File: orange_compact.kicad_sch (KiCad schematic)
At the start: 303 parts, among them IC1 MCP25625-E_ML, IC2 MIC5317-1.8YD5-TR, IC3 CD4060BPWR, IC4 MAX13487EESA+T, IC5 MCP73833T-FCI/MF, J1 Battery, J4 Conn_Coaxial, J4 USB_B_Micro, J5 Conn_01x08_Pin, J6 USB_B_Micro, Q1 MMBT3904, Q12 Q_NPN_BEC_BRT, Q2 MMBT3904, Q2 Q_NPN_BEC_BRT, Q3 MMBT3904, Q5 Q_NPN_BEC_BRT, Q6 Q_NPN_BEC_BRT, Q8 Q_NPN_BEC_BRT, SW1 SW_Push, SW2 SW_Push, U1 EG916QGLLG-N03-SGNSA, U10 LP5907MFX-3.3, U11 LM3671MF-3.3/NOPB, U12 AMS1117-1.8, U13 LIS2DH12TR, U14 LP5907MFX-1.8, U15 LM66100DCKR, U16 LM66100DCKR, U17 TPS3828-33DBVRG4, U18 TPS61022, U2 MDBT50Q-1M, U20 TPS566242DRLR, U21 SN74LVC1G14DBV, U22 TP4056, U23 MCP2515-xST, U24 MCP2562-E-MF, U25 ESP32-S3-MINI-1, U26 MCP2562-E/MF, U29 TXB0108RGY, U3 FDMC86139P, U30 TXB0104RUT, U4 LM5012DDAR, U6 LMR14030SDDAR, U7 LP5907MFX-3.3, U8 1NCE IoT SIMs Chip, U9 USBLC6-2SC6, Y1 16MHz

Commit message: done before gnd optimization
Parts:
- removed J5: Conn_01x08_Pin, Connector_JST:JST_XH_S8B-XH-A_1x08_P2.50mm_Horizontal, symbol Connector:Conn_01x08_Pin
- removed L12: 1uH, Inductor_SMD:L_Coilcraft_XAL4020-XXX, symbol Device:L
- removed L14: L_Ferrite_Coupled_1243, Inductor_SMD:L_CommonModeChoke_Laird_CMA0805, symbol Device:L_Ferrite_Coupled_1243
- removed R51: 22k, Resistor_SMD:R_0805_2012Metric, symbol Device:R_Small
- removed R55, R56: 0, Resistor_SMD:R_0402_1005Metric, symbol Device:R
- removed TH1: DNP, Resistor_SMD:R_0603_1608Metric, symbol Device:Thermistor_NTC
- added C119, C120: 1uF, Capacitor_SMD:C_0402_1005Metric, symbol Device:C
- added C72, C73: 100nF, Capacitor_SMD:C_0402_1005Metric, symbol Device:C
- added D17: BAT54AW, Package_TO_SOT_SMD:SOT-323_SC-70, symbol Diode:BAT54AW
- added D18: SM712_SOT23, Package_TO_SOT_SMD:SOT-323_SC-70, symbol Diode:SM712_SOT23
- added D20, D21, D22, D24: D4V5H1BS2LP-7B, Diode_SMD:D_0402_1005Metric, symbol Device:D_Zener
- added J7: Conn_01x11_Pin, Connector_PinHeader_2.00mm:PinHeader_1x11_P2.00mm_Vertical, symbol Connector:Conn_01x11_Pin
- added L15: 2.2uH, Inductor_SMD:L_0603_1608Metric, symbol Device:L
- added R57: 680, Resistor_SMD:R_0805_2012Metric, symbol Device:R_Small
- added R60: 1k, Resistor_SMD:R_0402_1005Metric, symbol Device:R_Small
- added R61: 130, Resistor_SMD:R_0603_1608Metric, symbol Device:R_Small
- added TP18: TestPoint, TestPoint:TestPoint_Pad_D1.0mm, symbol Connector:TestPoint
- added U19, U5: LTV-217, Package_SO:SOIC-4_4.55x2.6mm_P1.27mm, symbol TC-ICs:LTV-217
- added U27: LP5907MFX-3.3, Package_TO_SOT_SMD:SOT-23-5, symbol Regulator_Linear:LP5907MFX-3.3
- added U28: USBLC6-2SC6, Package_TO_SOT_SMD:SOT-23-6, symbol Power_Protection:USBLC6-2SC6
- D10: footprint Package_TO_SOT_SMD:TO-277A_alt -> Diode_SMD:D_SMA; MPN V8P12-M3/86A -> RB058L150; desc DIODE SCHOTTKY 120V 8A TO277A -> DIODE SCHOTTKY 150V 3A PMDS
- R31: footprint Resistor_SMD:R_0805_2012Metric -> Resistor_SMD:R_0603_1608Metric; MPN RMCF0805FT330K -> 0603WAF3303T5E
- R32: value 22k -> 11k; footprint Resistor_SMD:R_0805_2012Metric -> Resistor_SMD:R_0603_1608Metric; MPN RMCF0805FT22K0 -> RTT031102FTP
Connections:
- net 3V3_ALWAYS_ON: no longer C112.2, C44.1, C45.1, JP3.1 (A), R37.1, R38.1, R58.2, R59.2, R60.2, U13.10 (VDD_IO), U13.2 (CS), U13.9 (VDD), U26.5 (Vio)
- net 4V7_BOOST: now also TP16.1
- net 5V0: now also C119.1, U27.1 (IN)
- net CAN_500_H: now also D12.1 (A1), U26.7 (CANH), J7.7 (Pin_7); no longer D12.2 (A2)
- net CAN_500_L: now also D12.2 (A2), U26.6 (CANL), J7.6 (Pin_6); no longer D12.1 (A1)
- net D+/A: now also J7.8 (Pin_8)
- net D-/B: now also J7.9 (Pin_9)
- net GND: now also TP17.1, C119.2, C120.2, C72.2, C73.2, D17.3, D18.3 (common), D20.2 (A), D21.2 (A), D22.2 (A), D24.2 (A), J7.1 (Pin_1), J7.3 (Pin_3), L15.2, U19.3, U27.2 (GND), U28.2 (GND), U5.3
- net JTAG_D+: now also U28.1 (I/O1); no longer TP14.1
- net JTAG_D-: now also U28.3 (I/O2); no longer TP15.1
- net RXD0: now also D18.1 (A1), J7.5 (Pin_5); no longer TP17.1
- net STATUS_LED_3V3: now also U25.30 (IO48); no longer U25.32 (IO36)
- net TXD0: now also D18.2 (A2), J7.4 (Pin_4); no longer TP16.1
- net V_EXT: now also J7.2 (Pin_2)
- net at TP10.1, U1.23 (DBG_TXD): now also D22.1 (K)
- net IGN_IN: now reaches U25.31 (IO35)
- net IGN_IN: now also R60.2, U5.4
- net 3V3_LDO_EN: now reaches U25.8 (IO4)
- net 3V3_LDO_EN: now also U27.3 (EN)
- net at J4.1 (VBUS): now also U28.5 (VBUS)
- net at J4.2 (D-): now also TP14.1, U28.4 (I/O2)
- net at J4.3 (D+): now also TP15.1, U28.6 (I/O1)
- net at TP12.1, U1.96 (PSM_INT): now also D20.1 (K)
- net at TP13.1, U1.19 (AP_READY): now also D21.1 (K)
- net at TP11.1, U1.22 (DBG_RXD): now also D24.1 (K)
- new net: R57.2, U5.1
- new net: L15.1, U5.2
- new net: R61.2, U19.2
- new net 3V3_LDO: C112.2, C120.1, C44.1, C45.1, C72.1, C73.1, JP3.1 (A), R37.1, R38.1, R58.2, R59.2, R60.1, R60.2, TP18.1, U13.10 (VDD_IO), U13.2 (CS), U13.9 (VDD), U19.1, U26.5 (Vio), U27.5 (OUT)
- new net IGN: D17.1, J7.10 (Pin_10), R57.1
- new net IM_IN: R61.1, U25.32 (IO36)
- new net IM_OUT: D17.2, J7.11 (Pin_11), U19.4
- no-connect marks 69 -> 65
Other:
- note added: "ACTIVE_LOW"
- note added: "If = 15mA"
- note added: "If = 15mA STM32F105RB suck current limit = 25mA"
- note added: "Immobilizer & Ignition detect"
- note added: "Power dissipation R64 = 153mW"
- note added: "Vf = 1.4V GPIO_5 IGN_INPUT = 12 V (12V-1.4V)/0.015A =~ 680 Ohm"
- note removed: "10k (103A) Normaly inside battery"
- moved on the sheet: C101, C11, C112, C113, C14, C24, C3, C4, C46, C47, C57, C58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

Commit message: printed on JLC
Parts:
- removed C1, C6: 10uF, Capacitor_SMD:C_0603_1608Metric, symbol Device:C_Small
- removed C106, C107: 1uF, Capacitor_SMD:C_0603_1608Metric, symbol Device:C
- removed C12: 1nF, Capacitor_SMD:C_0402_1005Metric, symbol Device:C_Small
- removed C16, C17: 2u2, Capacitor_SMD:C_1210_3225Metric, symbol Device:C_Small
- removed C18, C20, C22: 0.1uF, Capacitor_SMD:C_0603_1608Metric, symbol Device:C_Small
- removed C19, C21: 4.7u, Capacitor_SMD:C_1210_3225Metric, symbol Device:C_Small
- removed C23, C41, C55, C7, C8: 100nF, Capacitor_SMD:C_0402_1005Metric, symbol Device:C_Small
- removed C25: 47u, Capacitor_SMD:C_1206_3216Metric, symbol Device:C_Small
- removed C26: 2.2n, Capacitor_SMD:C_0402_1005Metric, symbol Device:C_Small
- removed C27: 100p, Capacitor_SMD:C_0603_1608Metric, symbol Device:C_Small
- removed C28: 3.3n, Capacitor_SMD:C_0402_1005Metric, symbol Device:C_Small
- removed C30, C31, C53, C56: 22u, Capacitor_SMD:C_0603_1608Metric, symbol Device:C_Small
- removed C33, C34, C40: 10u, Capacitor_SMD:C_1206_3216Metric, symbol Device:C_Small
- removed C36, C38: 22uF, Capacitor_SMD:C_0805_2012Metric, symbol Device:C_Small
- removed C59, C74, C75, C97: 1uF, Capacitor_SMD:C_0402_1005Metric, symbol Device:C_Small
- removed C7, C8: 18pF, Capacitor_SMD:C_0402_1005Metric, symbol Device:C_Small
- removed D2: SM712_SOT23, Package_TO_SOT_SMD:SOT-323_SC-70, symbol Diode:SM712_SOT23
- removed D26: D5V0L4B5TS (5V), Package_TO_SOT_SMD:SOT-23-5, symbol Power_Protection:SP0504BAHT
- removed D6: SMCJ75A, digikey-footprints:DO-214AB, symbol Diode:1N62xxCA
- removed D7: D_Schottky, Package_TO_SOT_SMD:TO-277A_alt, symbol Device:D_Schottky
- removed D8: MM3Z18VT1G, Diode_SMD:D_SOD-323F, symbol Diode:MM3Zxx
- removed F1: 2A, Fuse:Fuse_1206_3216Metric, symbol Device:Fuse
- removed FB1: FerriteBead_Small, Resistor_SMD:R_1206_3216Metric, symbol Device:FerriteBead_Small
- removed IC1: MCP25625-E_ML, Package_DFN_QFN:QFN-28-1EP_6x6mm_P0.65mm_EP4.25x4.25mm, symbol TC-ICs:MCP25625-E_ML_OPTO
- removed IC2: MIC5317-1.8YD5-TR, TC-ICs:SOT95P280X130-5N, symbol TC-ICs:MIC5317-1.8YM5
- removed IC3: CD4060BPWR, SOP65P640X120-16N, symbol TC-ICs:CD4060BPWR
- removed IC5: MCP73833T-FCI/MF, TC-ICs:SON50P300X300X100-11N-D, symbol TC-ICs:MCP73833-CNI_MF
- removed L1: CMA0805A681R-1A, Inductor_SMD:L_CommonModeChoke_Laird_CMA0805, symbol Device:L_Ferrite_Coupled_1243
- removed L2: 8.2u, Inductor_SMD:L_Coilcraft_XxL4020, symbol Device:L_Small
- removed L3: 22u, Inductor_SMD:L_10.4x10.4_H4.8, symbol Device:L_Small
- removed L5: 2.2uH, Inductor_SMD:L_Taiyo-Yuden_MD-3030, symbol Device:L_Small
- removed Q1: MMBT3904, Package_TO_SOT_SMD:SOT-23, symbol Transistor_BJT:MMBT3904
- removed R1, R32, R9: 10k, Resistor_SMD:R_0402_1005Metric, symbol Device:R_Small
- removed R11: 20k, Resistor_SMD:R_1206_3216Metric, symbol Device:R_Small
- removed R14: 220k, Resistor_SMD:R_0805_2012Metric, symbol Device:R_Small
- removed R16: 330k, Resistor_SMD:R_0805_2012Metric, symbol Device:R_Small
- removed R17, R18: 120k, Resistor_SMD:R_0805_2012Metric, symbol Device:R_Small
- removed R19: 10k, Resistor_SMD:R_0402_1005Metric, symbol Device:R
- removed R2, R52: 100k, Resistor_SMD:R_0402_1005Metric, symbol Device:R
- removed R20: 41k2, Resistor_SMD:R_0603_1608Metric, symbol Device:R_Small
- removed R21: 182k, Resistor_SMD:R_0805_2012Metric, symbol Device:R_Small
- removed R23, R24: 2k8, Resistor_SMD:R_0402_1005Metric, symbol Device:R_Small
- removed R25, R26: 1.4, Resistor_SMD:R_0805_2012Metric, symbol Device:R_Small
- removed R29: 158k, Resistor_SMD:R_0603_1608Metric, symbol Device:R_Small
- removed R3: 1M, Resistor_SMD:R_0402_1005Metric, symbol Device:R
- removed R34: 220k, Resistor_SMD:R_0402_1005Metric, symbol Device:R
- removed R46: 1k, Resistor_SMD:R_0402_1005Metric, symbol Device:R_Small
- removed R49: 49k9, Resistor_SMD:R_0603_1608Metric, symbol Device:R_Small
- removed R81, R82: 4K7, Resistor_SMD:R_0603_1608Metric, symbol Device:R_Small
- removed R83: 2k, Resistor_SMD:R_0603_1608Metric, symbol Device:R_Small
- removed U11: LM3671MF-3.3/NOPB, Package_TO_SOT_SMD:SOT-23-5, symbol TC-Power:LM3671MFX-1.8
- removed U12: AMS1117-1.8, Package_TO_SOT_SMD:SOT-223-3_TabPin2, symbol Regulator_Linear:AMS1117-1.8
- removed U2: MDBT50Q-1M, TC-RF-module:MDBT50Q-1M, symbol TC-RF-Module:MDBT50Q-1M
- removed U23: MCP2515-xST, Package_SO:TSSOP-20_4.4x6.5mm_P0.65mm, symbol Interface_CAN_LIN:MCP2515-xST
- removed U24: MCP2562-E-MF, Package_DFN_QFN:DFN-8-1EP_3x3mm_P0.65mm_EP1.55x2.4mm, symbol Interface_CAN_LIN:MCP2562-E-MF
- removed U3: FDMC86139P, TC-ICs:WDFN8-511DH-O_3p3x3p3x0p65_OSI, symbol TC-Transistors:FDMC86139P
- removed U4: LM5012DDAR, Package_SO:SOIC-8-1EP_3.9x4.9mm_P1.27mm_EP2.95x4.9mm_Mask2.71x3.4mm_ThermalVias_variant, symbol Regulator_Switching:LM5017MR
- removed Y1: 16MHz, Crystal:Crystal_SMD_Abracon_ABM8G-4Pin_3.2x2.5mm, symbol Device:Crystal_GND24
- C103, C104: value 47UF -> 22UF; MPN GRM21BR61A226ME44L** -> LMK212BJ226MG-T**
- C11: footprint Capacitor_SMD:C_2220_5750Metric -> Capacitor_SMD:C_1210_3225Metric
- C24: MPN GRM155R71C822KA01D -> GRM155R71C103KA01D**
- C47: value 270pF -> 220pF; MPN GRM033R71C271KA01D -> GRM033R71C221KA01D**
- C79: MPN GCM155R72A102KA37D -> GCM188R72A102KA37D
- D10: MPN RB058L150 -> RB058L150TE25
- L11: footprint Inductor_SMD:L_Coilcraft_XAL4020-XXX -> TC-Inductor:IND_SPM5030T-1R0M; Field5 XAL4020-102MEC -> SPM5030T-1R0M
- R50: MPN (none) -> RMCF0402ZT0R00
- R86: value 4K -> 3.9K
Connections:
- net 3V3_ALWAYS_ON: now also C44.1, C45.1, R37.1, R38.1, U13.10 (VDD_IO), U13.2 (CS), U13.9 (VDD)
- net 3V3_LDO: no longer C44.1, C45.1, R37.1, R38.1, U13.10 (VDD_IO), U13.2 (CS), U13.9 (VDD)
- net IBL: now also TP3.1
- net VBAT: no longer TP3.1
- no-connect marks 65 -> 31
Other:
- note added: "3.3V LDO"
- note added: "VEN = 1.2V"
- note removed: "2k = 500mA max charge current"
- note removed: "3.3V Buck"
- note removed: "33u electrolyte replacement with 0.7Ohm fixed ESR to keep filter damping"
- note removed: "8-60 VIN to 5V"
- note removed: "Always active mode"
- note removed: "BECOME SO EXPENSIVE AGAIN"
- note removed: "CD4060 is a 14 bit counter with internal oscillator Oscillator setup with C and R as below: f = 1 / ( 2.5 x R x C) f = 1 / (2.5 * 220k * 1u) = 1.8Hz 1/1.8Hz = 0.55 sec 0b10000000000000 = 8192 0.55sec * 8192 = ~75min Q13 is turned HIGH after around 75min toggle WDI will reset counter Power cycle will reset counter SHALL WE KEEP IT?"
- note removed: "Crazy watchdog circuit"
- note removed: "ESD prot"
- note removed: "F3 If need lower res: 0468002.NR"
- note removed: "I2C1"
- note removed: "MODEM"
- note removed: "Power limit resistor"
- note removed: "R61 dissipation = (60V-18V)^2 / 20k = 88mW 1206 250mW"
- note removed: "Reset time will depend on nominal VIN voltage and need to be adjusted if nominal voltage is changed"
- note removed: "TODO Doublecheck if usable for SW UART"
- note removed: "This is only to save height on the board If not important, replace with electrolyte will lower BOM cost"
- note removed: "U15 Max rDS(on) = 67 m at VGS = −10 V, ID = −4.4 A MAX VGS = 20V"
- note removed: "ULVO / EN PIN is turning off regulation below 1.5V Used as combined UV shutoff and board reset."
- note removed: "UVLO = ~9V Adjusted by R16 and R17//R49"
- note removed: "VIN / filter"
- note removed: "WDO HIGH pulse will discharge C53 and turn off U4 C53 will slowly recharge throu R16 and when reaching 1.5V U4 will turn on again. This will create a reset delay time of ~4sec."
- note removed: "peak discharge current ~70mA is set by base res (R50)"
- moved on the sheet: C100, C101, C102, C103, C104, C105, C108, C109, C110, C111, C115, C116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

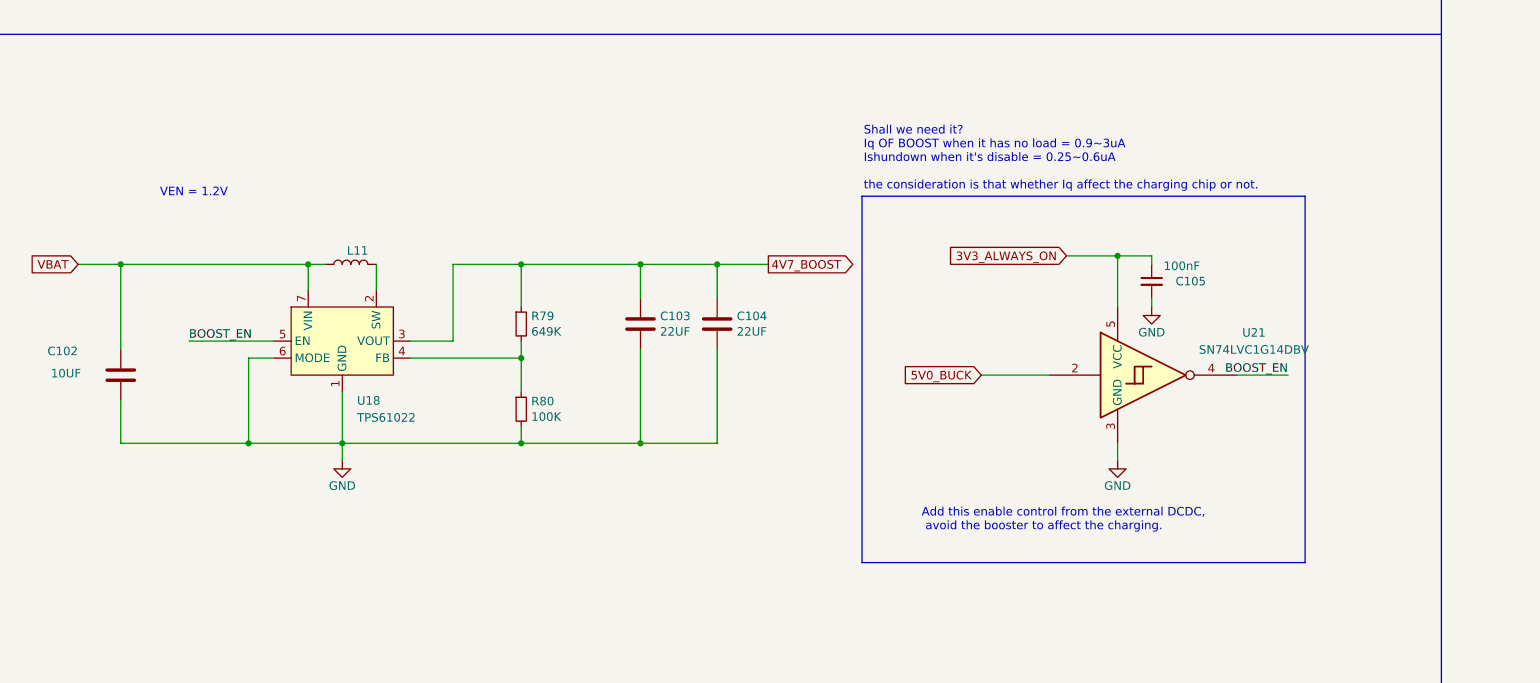
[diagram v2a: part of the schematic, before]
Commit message: delete SN74 for TPS61022
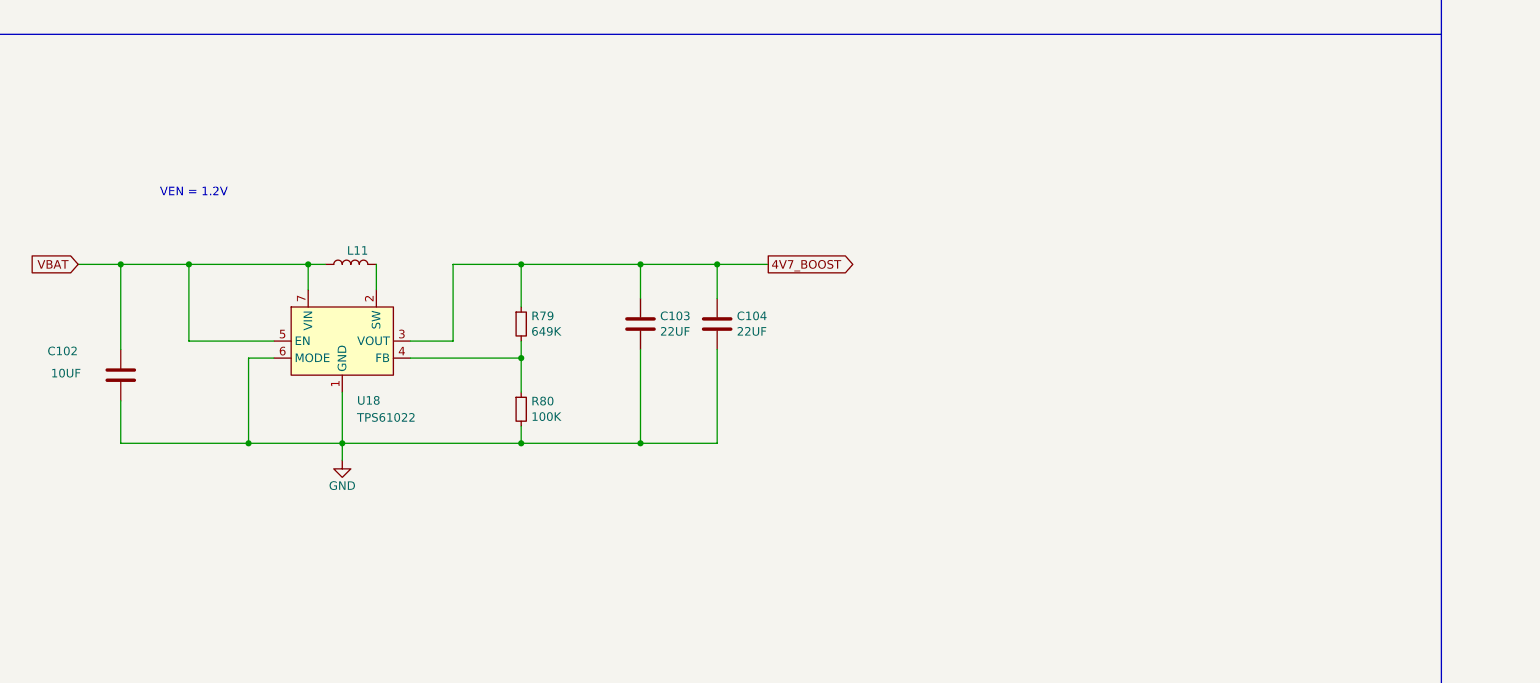
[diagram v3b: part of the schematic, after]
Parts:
- removed C105: 100nF, Capacitor_SMD:C_0402_1005Metric, symbol Device:C_Small
- removed U21: SN74LVC1G14DBV, Package_TO_SOT_SMD:SOT-23-5, symbol 74xGxx:SN74LVC1G14DBV
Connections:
- net BOOST_EN is gone; now on net VBAT: U18.5 (EN)
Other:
- note removed: "Add this enable control from the external DCDC, avoid the booster to affect the charging."
- note removed: "Shall we need it? Iq OF BOOST when it has no load = 0.9~3uA Ishundown when it's disable = 0.25~0.6uA the consideration is that whether Iq affect the charging chip or not."

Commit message: delete watchdog——TPS3828
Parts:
- removed C101: 100nF, Capacitor_SMD:C_0402_1005Metric, symbol Device:C_Small
- removed JP2: Jumper_2_Bridged, Jumper:SolderJumper-2_P1.3mm_Bridged2Bar_RoundedPad1.0x1.5mm, symbol Jumper:Jumper_2_Bridged
- removed R50: 0, Resistor_SMD:R_0402_1005Metric, symbol Device:R_Small
- removed U17: TPS3828-33DBVRG4, Package_TO_SOT_SMD:SOT-23-5, symbol TC-ICs:TPS3828-33DBVRG4
- R87: MPN 0603WAF500LT5E -> (none)
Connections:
- net WDO: no longer names the net of R27.2, R28.1, U6.3 (EN)
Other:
- note added: "600MA*600mA*0.5 = 180mW"
- note added: "R87 for pre-thermal release for internal LDO of TP4056 TP4056X 应用在大电流充电（700mA 以上），为了缩短充电时间，需增加热 耗散电阻，阻值范围 0.2～0.5Ω。客户根据使用情况选取合适电阻大小"
- note removed: "15uA OPEN-DRAIN ACTIVE-LOW 1RMB SMALL SIZE"
- note removed: "R87 for pre-thermal release for internal LDO of TP4056"
- moved on the sheet: C102, C103, C104, L11, R79, R80, U18
